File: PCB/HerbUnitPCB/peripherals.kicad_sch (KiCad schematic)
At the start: 7 parts, among them SW3 SW_Push

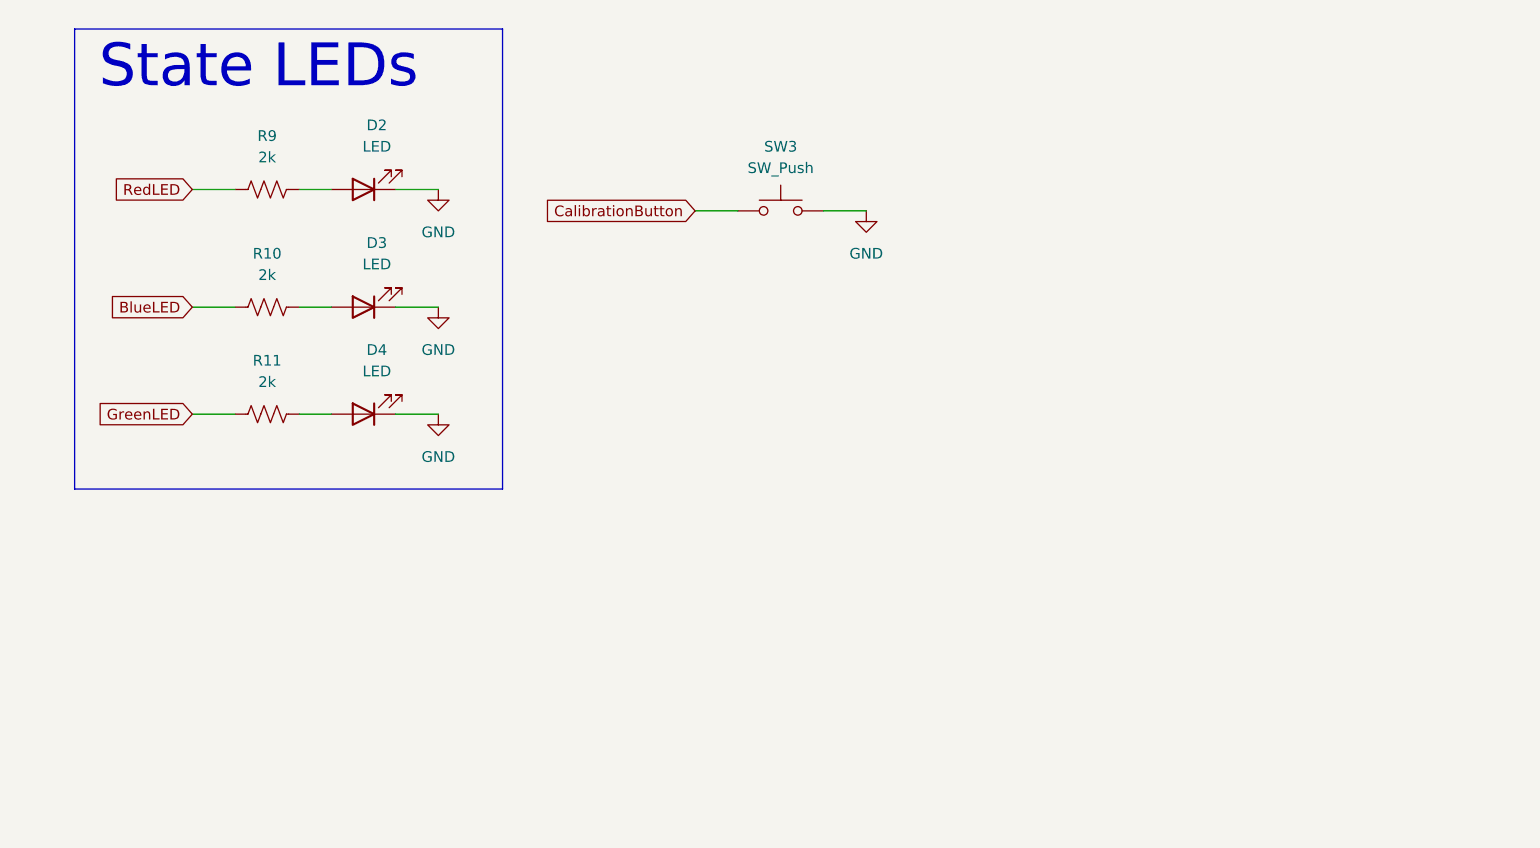
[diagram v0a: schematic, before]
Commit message: Peripherals
Finished most of the Peripherals.
- Added temp sensor
- Added Moisture sensor
- Added float switch
- Added SD card reader/writer
- Still need to add barrel jack/pump
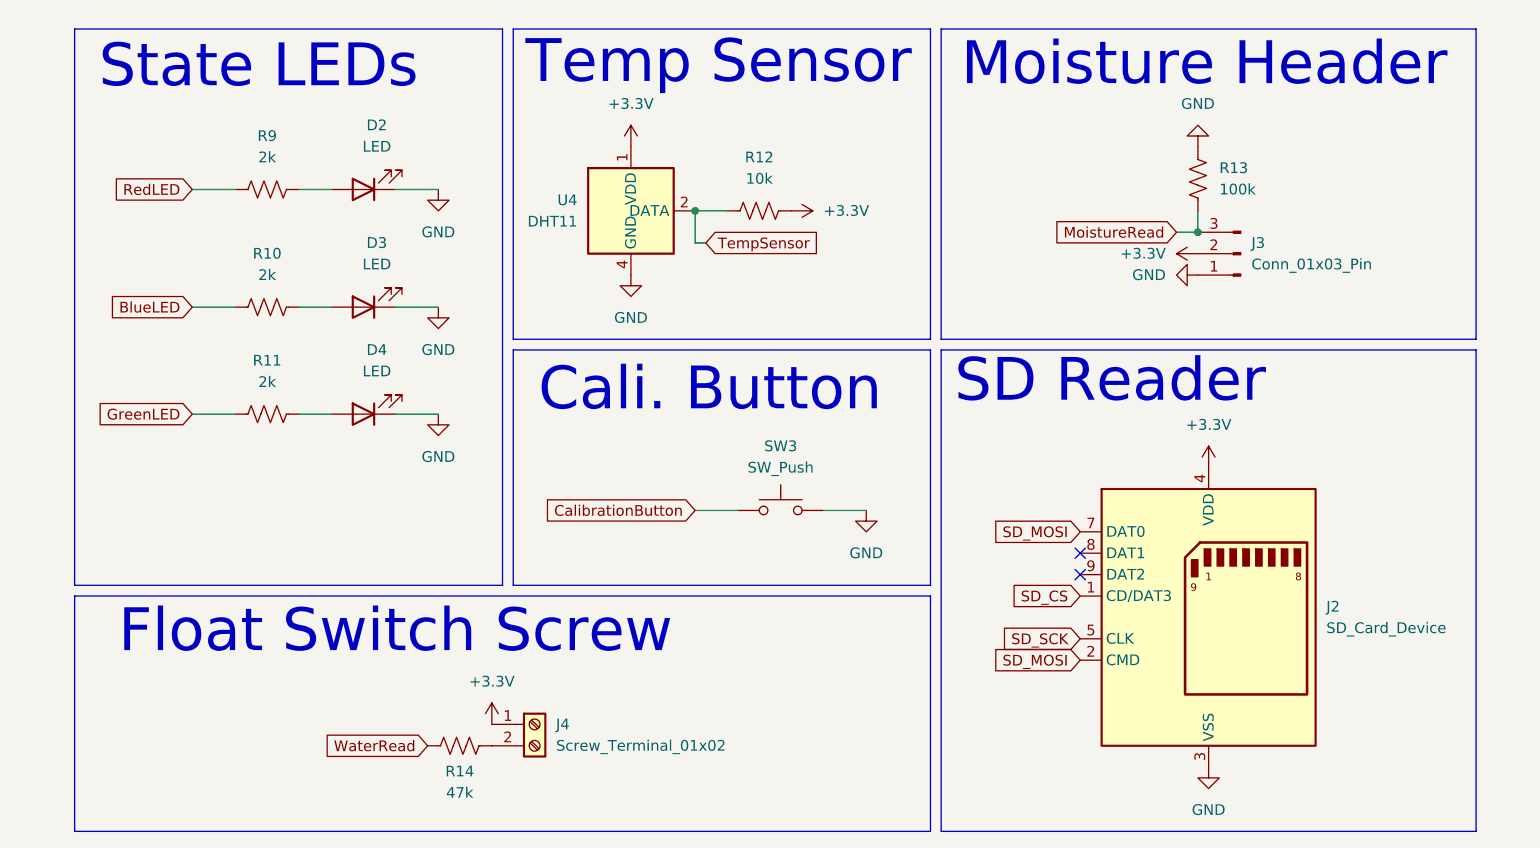
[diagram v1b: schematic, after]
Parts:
- added J2: SD_Card_Device, Connector_Card:SD_Card_Device_16mm_SlotDepth, symbol Connector:SD_Card_Device
- added J3: Conn_01x03_Pin, symbol Connector:Conn_01x03_Pin
- added J4: Screw_Terminal_01x02, symbol Connector:Screw_Terminal_01x02
- added R12: 10k, Resistor_SMD:R_0402_1005Metric, symbol Device:R_US
- added R13: 100k, Resistor_SMD:R_0402_1005Metric, symbol Device:R_US
- added R14: 47k, Resistor_SMD:R_0402_1005Metric, symbol Device:R_US
- added U4: DHT11, Sensor:Aosong_DHT11_5.5x12.0_P2.54mm, symbol Sensor:DHT11
- SW3: footprint (none) -> Button_Switch_SMD:SW_Push_1P1T_NO_CK_PTS125Sx43PSMTR
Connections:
- net GND: now also J2.3 (VSS), J2.6 (VSS), J3.1 (Pin_1), R13.2, U4.4 (GND)
- new net: J4.2 (Pin_2), R14.2
- new net +3.3V: J2.4 (VDD), J3.2 (Pin_2), J4.1 (Pin_1), R12.2, U4.1 (VDD)
- new net MoistureRead: J3.3 (Pin_3), R13.1
- new net SD_CS: J2.1 (CD/DAT3)
- new net SD_MOSI: J2.2 (CMD), J2.7 (DAT0)
- new net SD_SCK: J2.5 (CLK)
- new net TempSensor: R12.1, U4.2 (DATA)
- new net WaterRead: R14.1
- no-connect marks 0 -> 2
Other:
- note added: "Cali. Button"
- note added: "Float Switch Screw"
- note added: "Moisture Header"
- note added: "SD Reader"
- note added: "Temp Sensor"
- moved on the sheet: SW3
